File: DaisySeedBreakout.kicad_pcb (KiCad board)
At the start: 4 copper layers, 47.9 x 53.6 mm, 93 parts, among them J1 Conn_01x03, J10 Conn_01x03, J11 Conn_01x02, J12 Conn_01x02, J13 Conn_01x02, J14 Conn_01x03, J15 Conn_01x03, J16 Conn_01x02, J17 Conn_01x02, J2 Conn_01x02, J3 Conn_01x03, J4 5027740891, J5 Conn_02x08, J6 Pins_02x10_P2.54mm_TH, J7 Conn_01x10, J9 Conn_01x02, U1 H11L1M, U10 TPD2EUSB30ADRTR, U2 MAX4466EXK_T, U7 TLV9062IDR

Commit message: periodic update
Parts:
- removed C16: 10U, Capacitor_SMD:C_0805_2012Metric
- removed J7: Conn_01x10, Connector_PinHeader_2.54mm:PinHeader_1x10_P2.54mm_Vertical
- removed R29: 4.7k, Resistor_SMD:R_0402_1005Metric
- added J8: Conn_01x02, 1x2FemaleVertical:PinHeader_1x02_P2.54mm_VerticalFemale, F.Cu at (133.1, 60.3)
- C13, C7, D1, R21, R30, R54, R55: moved to B.Cu
- C15: value 10U -> 0.1uF; footprint Capacitor_SMD:C_0805_2012Metric -> Capacitor_SMD:C_0603_1608Metric
- C24, C70, C71, R66, R8, U3: moved to F.Cu
- J1, J10, J14, J3: footprint Ultralibrarian:PinHeader_1x03_P2.54mm_Vertical_Female -> HeadersWithSolderHoles:PinHeader_1x03_P2.54mm_Vertical_Female_WithSolderHoles
- J11, J12, J13, J17, J2: footprint 1x2FemaleVertical:PinHeader_1x02_P2.54mm_VerticalFemale -> HeadersWithSolderHoles:PinHeader_1x02_P2.54mm_VerticalFemale_WithSolderHoles
- J15: footprint Ultralibrarian:PinHeader_1x03_P2.54mm_Vertical_Female -> Connector_PinHeader_2.54mm:PinHeader_1x03_P2.54mm_Vertical
- J5: footprint Connector_PinHeader_2.54mm:PinHeader_2x08_P2.54mm_Vertical -> HeadersWithSolderHoles:PinHeader_2x08_P2.54mm_Vertical_Female
- J6: value Pins_02x10_P2.54mm_TH -> Conn_01x02; footprint Connector_PinHeader_2.54mm:PinHeader_2x10_P2.54mm_Vertical -> 1x2FemaleVertical:PinHeader_1x02_P2.54mm_VerticalFemale
- J9: value Conn_01x02 -> Pins_02x10_P2.54mm_TH; footprint 1x2FemaleVertical:PinHeader_1x02_P2.54mm_VerticalFemale -> HeadersWithSolderHoles:PinHeader_3x10_P2.54mm_Vertical
- moved J16 68.3 mm to (186.1, 88.3)
- moved C10 56.6 mm to (191.8, 97.0), turned to -90 degrees
- moved C6 45.7 mm to (112.4, 100.5)
- moved R11 41.6 mm to (102.7, 88.9)
- moved J12 41.4 mm to (130.6, 45.7), turned to 0 degrees
- moved J13 41.4 mm to (133.1, 45.7), turned to 0 degrees
- moved J5 38.5 mm to (157.5, 36.2)
- moved R52 35.7 mm to (116.6, 103.4)
- moved R53 35.7 mm to (116.3, 101.6)
- moved R6 34.9 mm to (108.4, 89.2)
- moved C15 32.4 mm to (143.3, 39.6), turned to -90 degrees
- moved J11 30.9 mm to (130.6, 73.2), turned to 0 degrees
- moved J1 29.2 mm to (137.2, 86.9)
- moved J2 28.9 mm to (133.1, 73.2), turned to 0 degrees
- moved J9 28.7 mm to (157.5, 56.5), turned to 0 degrees
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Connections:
- net /Audio In Sum/AUDIO_IN_L_CONN renamed /Audio In/AUDIO_IN_L_CONN
- net /Audio In Sum/AUDIO_IN_L_SUMMED renamed /Audio In/AUDIO_IN_L_SUMMED
- net /Audio In Sum/AUDIO_IN_R_CONN renamed /Audio In/AUDIO_IN_R_CONN
- net /Audio In Sum/AUDIO_IN_R_SUMMED renamed /Audio In/AUDIO_IN_R_SUMMED
- net Net-(C27-Pad2) renamed /Condensor Microphone/AUDIO_OUT
- A1 pad 39: unconnected-(A1-VIN-Pad39) -> Net-(A1-VIN)
- C15 pad 1: /Audio In Sum/AUDIO_IN_L_LOCAL -> Net-(A1-VIN)
- C15 pad 2: Net-(U7A-IN+) -> GND
- J15 pad 2: /USB_p -> /USB_n
- J15 pad 3: /USB_n -> /USB_p
- J6 pad 2: /AI_9 -> Net-(A1-VIN)
- J9 pad 1: /Audio In Sum/AUDIO_IN_R_LOCAL -> GND
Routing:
- net +3.3V: track 195.5 -> 6.27 mm, vias 7 -> 0
- net +3.3VA: track 101.7 -> 20.6 mm, vias 11 -> 2
- net /DIO6: track 49.9 -> 0.00 mm
- net /DIO7: track 45.8 -> 0.00 mm
- net /AI_0: track 43.4 -> 0.00 mm, vias 1 -> 0
- net /AI_2: track 42.5 -> 0.00 mm, vias 1 -> 0
- net GND: track 80.5 -> 38.7 mm, vias 44 -> 24
- net /AI_1: track 40.4 -> 0.00 mm, vias 1 -> 0
- net /AI_3: track 38.2 -> 0.00 mm, vias 1 -> 0
- net /AI_7: track 37.1 -> 0.00 mm, vias 1 -> 0
- net /AI_5: track 36.6 -> 0.00 mm, vias 1 -> 0
- net /AI_8: track 34.6 -> 0.00 mm, vias 1 -> 0
- net /AI_4: track 34.3 -> 0.00 mm, vias 1 -> 0
- net /AI_6: track 33.6 -> 0.00 mm, vias 1 -> 0
- net /DIO2: track 33.1 -> 0.54 mm
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- added copper zone on In1.Cu, net +3.3VA
- added copper zone on F.Cu, net GND
- removed copper zone on F.Cu, net +3.3V
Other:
- board size 47.9 x 53.6 mm -> 45.6 x 59.3 mm
- board text added: "AI0"
- board text added: "AI1"
- board text added: "AI2"
- board text added: "AI3"
- board text added: "AI4"
- board text added: "AI5"
- board text added: "AI6"
- board text added: "AI7"
- board text added: "AI8"
- board text added: "AI9"
- board text added: "AO0"
- board text added: "AO1"
- board text added: "D0/SCL/RX"
- board text added: "D1/SDA/TX"
- board text added: "D2/SPI_CS"
- board text added: "D3/SPI_CLK"
- board text added: "D4/SPI_POCI"
- board text added: "D5/SPI_PICO"
- board text added: "D6"
- board text added: "D7"
- board text added: "GND,VIN"
- board text added: "IN L"
- board text added: "IN R"
- board text added: "MIDI In"
- board text added: "MIDI Out"
- board text added: "Mic"
- board text added: "Mic Enable"
- board text added: "OUT L"
- board text added: "OUT R"
- board text added: "USB/TXRX"
- board text removed: "0 1 2 3 4 5 6 7 8 9 A B C D E F"
- board text removed: "7 6 5 4 3 2 1 0"
- board text removed: "9 8 7 6 5 4 3 2 1 0"
- board text removed: "Analog O"
- board text removed: "GND AI 3.3VA"
- board text removed: "GND AO 3.3V"
- board text removed: "GND AudI"
- board text removed: "GND AudIAux"
- board text removed: "GND AudO"
- board text removed: "GND, 3.3VD"
- board text removed: "L R"
- board text removed: "MIDI IN"
- board text removed: "MIDI OUT"
- board text removed: "Microphone"
- board text removed: "R"
- board text removed: "USB Host"

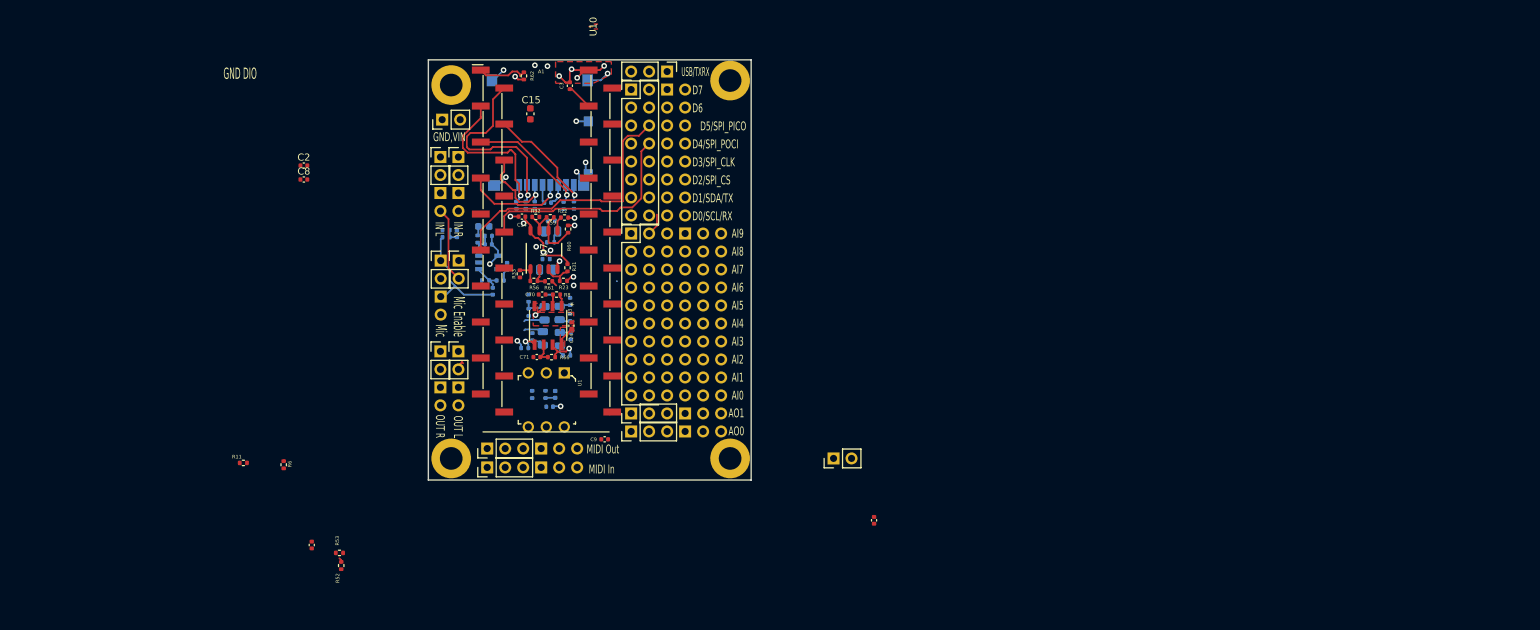
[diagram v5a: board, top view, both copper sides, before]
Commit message: added dedicated SPI, UART, I2C connectors
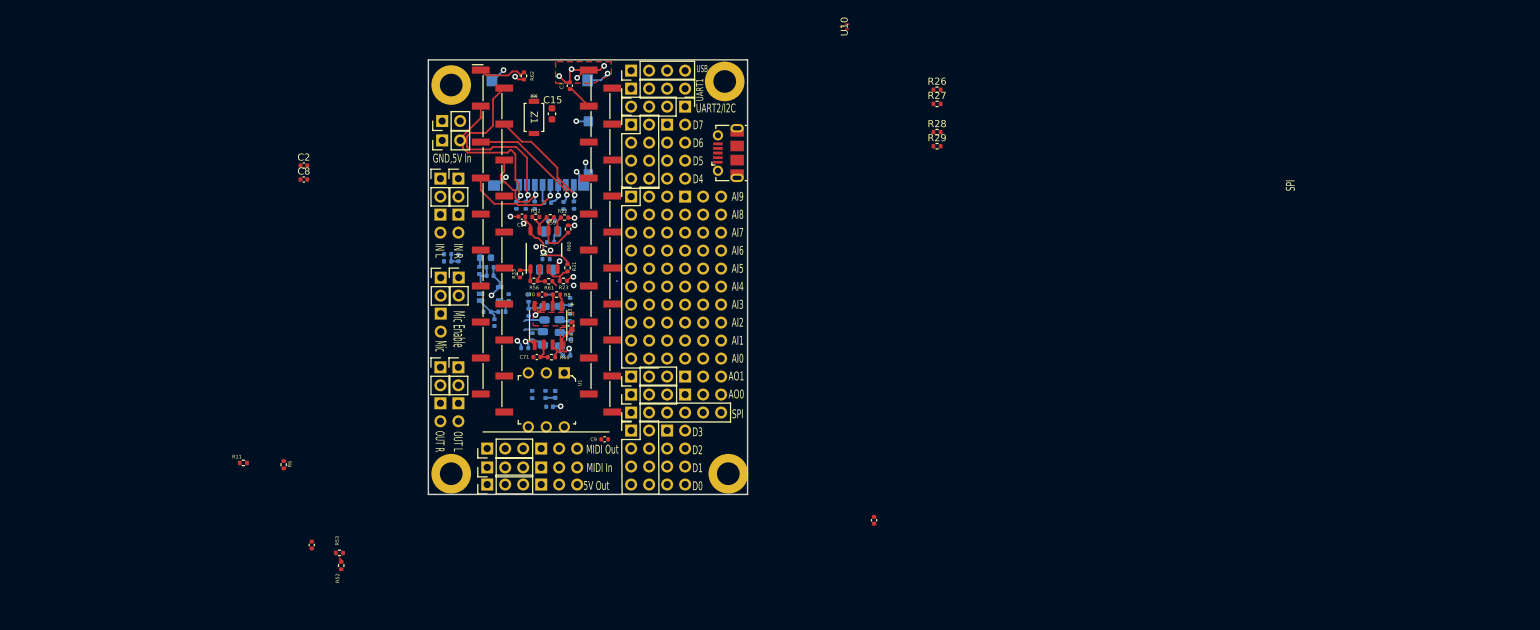
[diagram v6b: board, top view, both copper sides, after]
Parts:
- added J18: Conn_02x04, HeadersWithSolderHoles:PinHeader_2x04_P2.54mm_Vertical_Female, F.Cu at (157.5, 41.1)
- added J19: Conn_01x06, Ultralibrarian:PinHeader_1x06_P2.54mm_Vertical_Female, F.Cu at (157.5, 81.8)
- added J20: Conn_01x04, FemaleHeaders:PinHeader_1x04_P2.54mm_Vertical_Female, F.Cu at (157.5, 36.1)
- added J21: Conn_02x04, HeadersWithSolderHoles:PinHeader_2x04_P2.54mm_Vertical_Female, F.Cu at (157.5, 84.3)
- added J22: Conn_01x02, 1x2FemaleVertical:PinHeader_1x02_P2.54mm_VerticalFemale, F.Cu at (130.8, 43.4)
- added J7: Conn_01x04, FemaleHeaders:PinHeader_1x04_P2.54mm_Vertical_Female, F.Cu at (165.1, 38.6)
- added R26: DNP, Resistor_SMD:R_0402_1005Metric, F.Cu at (200.7, 36.2)
- added R27: DNP, Resistor_SMD:R_0402_1005Metric, F.Cu at (200.7, 38.2)
- added R28: DNP, Resistor_SMD:R_0402_1005Metric, F.Cu at (200.7, 42.2)
- added R29: DNP, Resistor_SMD:R_0402_1005Metric, F.Cu at (200.7, 44.2)
- added Z1: RSX501LAM20TR, 5ADiode:DIO_RB050LAM_ROM, F.Cu at (143.8, 40.1)
- J15: value Conn_01x03 -> USB_B_Micro; footprint Connector_PinHeader_2.54mm:PinHeader_1x03_P2.54mm_Vertical -> Connector_USB:USB_Micro-B_Molex-105017-0001
- J16: value Conn_01x02 -> Conn_01x03; footprint 1x2FemaleVertical:PinHeader_1x02_P2.54mm_VerticalFemale -> HeadersWithSolderHoles:PinHeader_1x03_P2.54mm_Vertical_Female_WithSolderHoles
- J5: value Conn_02x08 -> Conn_01x04; footprint HeadersWithSolderHoles:PinHeader_2x08_P2.54mm_Vertical_Female -> FemaleHeaders:PinHeader_1x04_P2.54mm_Vertical_Female
- moved J16 49.0 mm to (137.2, 91.9)
- moved U10 35.5 mm to (187.6, 27.3)
- moved J15 14.4 mm to (171.2, 45.2), turned to 90 degrees
- moved J14 5.21 mm to (157.5, 76.7)
- moved J9 5.21 mm to (157.5, 51.3)
- moved J10 5.21 mm to (157.5, 79.2)
- moved C28 4.43 mm to (136.9, 59.9)
- moved C23 4.43 mm to (140.2, 65.6)
- moved C27 4.43 mm to (137.6, 62.5)
- moved R17 4.43 mm to (137.6, 61.3)
- moved R20 4.43 mm to (136.0, 61.7)
- moved U2 4.43 mm to (137.6, 65.0)
- moved R16 4.43 mm to (137.2, 67.6)
- moved R15 4.43 mm to (139.2, 67.6)
- moved C26 4.43 mm to (138.2, 69.1)
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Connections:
- A1 pad 10: /DIO4 -> /DIO2_POCI
- A1 pad 11: /DIO5 -> /DIO3_PICO
- A1 pad 12: /DIO0 -> /DIO4_SCL_RX
- A1 pad 13: /DIO1 -> /DIO5_SDA_TX
- A1 pad 8: /DIO2 -> /DIO0_CS
- A1 pad 9: /DIO3 -> /DIO1_SCK
- J15 pad 1: GND -> unconnected-(J15-VBUS-Pad1)
- J15 pad 2: /USB_n -> unconnected-(J15-D--Pad2)
- J15 pad 3: /USB_p -> unconnected-(J15-D+-Pad3)
- J16 pad 1: GND -> +5V
- J16 pad 2: +3.3V -> +5V
- J5 pad 1: GND -> unconnected-(J5-Pin_1-Pad1)
- J5 pad 2: /DIO7 -> GND
- J5 pad 3: GND -> /USB_n
- J5 pad 4: /DIO6 -> /USB_p
- J6 pad 2: Net-(A1-VIN) -> Net-(J22-Pin_2)
- R11 pad 2: /DIO0 -> /DIO4_SCL_RX
- R6 pad 2: /DIO1 -> /DIO5_SDA_TX
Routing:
- net /DIO5: track 37.8 -> 0.00 mm
- net /DIO4: track 31.1 -> 0.00 mm
- net Net-(J17-Pin_1): track 16.3 -> 0.00 mm
- net /Audio In/AUDIO_IN_L_CONN: track 10.6 -> 0.00 mm
- net +3.3VA: track 20.6 -> 17.5 mm
- net GND: track 38.7 -> 38.2 mm, vias 24 -> 22
- net /DIO2: track 0.54 -> 0.00 mm
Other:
- board size 45.6 x 59.3 mm -> 45.1 x 61.3 mm
- board text added: "5V Out"
- board text added: "D0"
- board text added: "D1"
- board text added: "D2"
- board text added: "D3"
- board text added: "D4"
- board text added: "D5"
- board text added: "GND,5V In"
- board text added: "SPI"
- board text added: "UART1"
- board text added: "UART2/I2C"
- board text added: "USB"
- board text removed: "D0/SCL/RX"
- board text removed: "D1/SDA/TX"
- board text removed: "D2/SPI_CS"
- board text removed: "D3/SPI_CLK"
- board text removed: "D4/SPI_POCI"
- board text removed: "D5/SPI_PICO"
- board text removed: "GND DIO"
- board text removed: "GND,VIN"
- board text removed: "USB/TXRX"

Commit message: Layout routed, no DRC yet
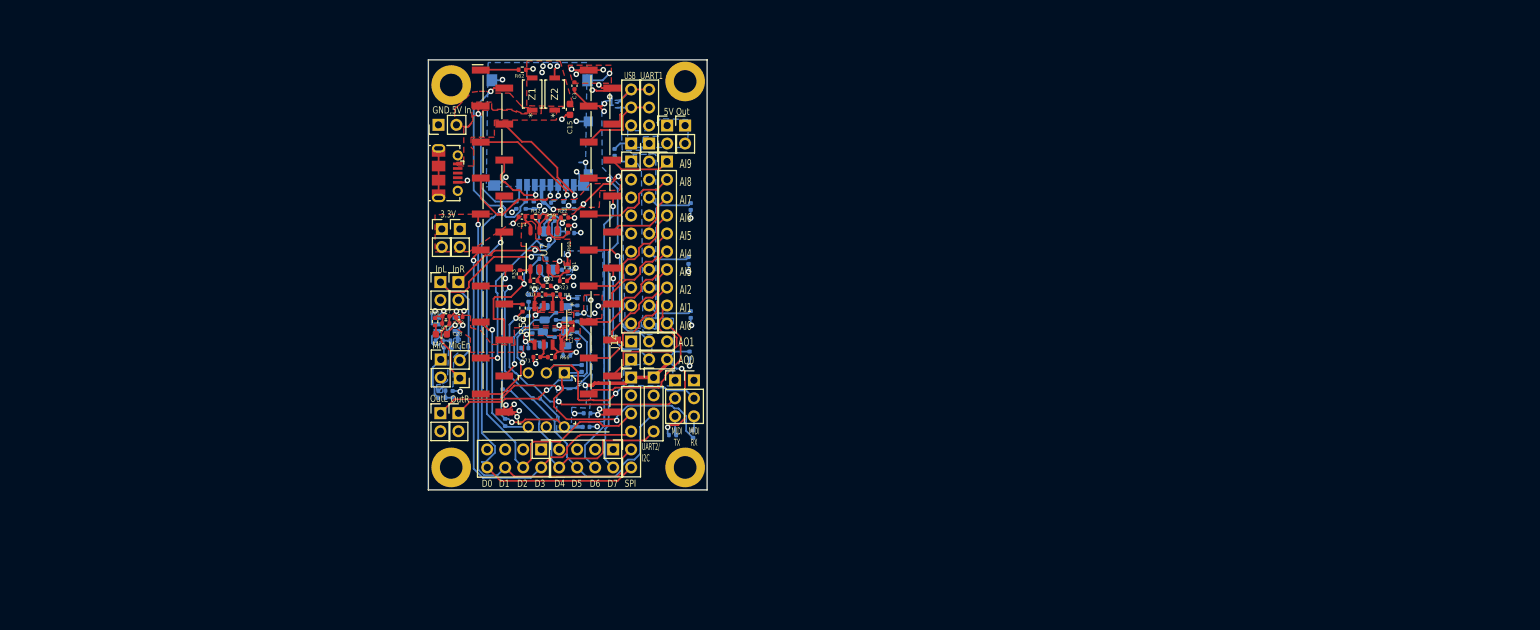
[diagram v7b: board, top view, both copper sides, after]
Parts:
- removed J22: Conn_01x02, 1x2FemaleVertical:PinHeader_1x02_P2.54mm_VerticalFemale
- added C16: 0.1uF, Capacitor_SMD:C_0402_1005Metric, B.Cu at (155.1, 45.1)
- added J23: Pins_02x10_P2.54mm_TH, 2x10FemaleHeader:PinHeader_2x10_P2.54mm_Vertical, F.Cu at (157.5, 46.4)
- added J24: Conn_01x10, Connector_PinHeader_2.54mm:PinHeader_1x10_P2.54mm_Vertical, F.Cu at (162.5, 46.4)
- added J25: Conn_01x02, 1x2FemaleVertical:PinHeader_1x02_P2.54mm_VerticalFemale, F.Cu at (130.8, 55.9)
- added J26: Conn_01x02, 1x2FemaleVertical:PinHeader_1x02_P2.54mm_VerticalFemale, F.Cu at (133.3, 55.9)
- added Z2: RSX501LAM20TR, 5ADiode:DIO_RB050LAM_ROM, F.Cu at (146.7, 36.8)
- C10, C2, C6, C8, C9, R11, R26, R27, R28, R29, R53, R6, U10: moved to B.Cu
- C23, C27, C28, R17, R20: moved to F.Cu
- J1, J10, J14, J3: footprint HeadersWithSolderHoles:PinHeader_1x03_P2.54mm_Vertical_Female_WithSolderHoles -> FemaleHeaders:PinHeader_1x03_P2.54mm_Vertical_Female
- J11, J12, J13, J17, J2: footprint HeadersWithSolderHoles:PinHeader_1x02_P2.54mm_VerticalFemale_WithSolderHoles -> 1x2FemaleVertical:PinHeader_1x02_P2.54mm_VerticalFemale
- J16: value Conn_01x03 -> Conn_01x02; footprint HeadersWithSolderHoles:PinHeader_1x03_P2.54mm_Vertical_Female_WithSolderHoles -> 1x2FemaleVertical:PinHeader_1x02_P2.54mm_VerticalFemale
- J18, J21: footprint HeadersWithSolderHoles:PinHeader_2x04_P2.54mm_Vertical_Female -> FemaleHeaders:PinHeader_2x04_P2.54mm_Vertical_Female
- J9: value Pins_02x10_P2.54mm_TH -> Conn_01x02; footprint HeadersWithSolderHoles:PinHeader_3x10_P2.54mm_Vertical -> 1x2FemaleVertical:PinHeader_1x02_P2.54mm_VerticalFemale
- moved C6 66.6 mm to (165.6, 60.3)
- moved R28 61.0 mm to (146.7, 70.6), turned to -90 degrees
- moved R26 60.5 mm to (145.0, 60.1)
- moved R29 58.9 mm to (146.9, 68.2), turned to 90 degrees
- moved R27 58.8 mm to (145.3, 58.2)
- moved J16 57.9 mm to (165.1, 41.3), turned to 0 degrees
- moved C8 57.8 mm to (165.9, 67.9), turned to -90 degrees
- moved C2 54.9 mm to (165.9, 52.7), turned to -90 degrees
- moved R53 49.9 mm to (163.3, 85.0), turned to 0 degrees
- moved J18 45.9 mm to (154.9, 87.0), turned to -90 degrees
- moved R52 44.5 mm to (142.2, 67.0), turned to -90 degrees
- moved J15 39.8 mm to (131.5, 48.0), turned to -90 degrees
- moved J7 38.5 mm to (160.7, 76.8), turned to 0 degrees
- moved R11 37.9 mm to (139.3, 79.0), turned to 90 degrees
- moved R6 36.9 mm to (144.1, 79.8), turned to 180 degrees
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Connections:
- A1 pad 39: Net-(A1-VIN) -> +5V
- C10 pad 1: +3.3VA -> +3.3V
- C15 pad 1: Net-(A1-VIN) -> +5V
- C2 pad 1: +3.3VA -> +3.3V
- C6 pad 1: +3.3VA -> +3.3V
- C8 pad 1: +3.3VA -> +3.3V
- J10 pad 3: +3.3VA -> +3.3V
- J14 pad 3: +3.3VA -> +3.3V
- J15 pad 1: unconnected-(J15-VBUS-Pad1) -> Net-(J15-VBUS)
- J5 pad 1: unconnected-(J5-Pin_1-Pad1) -> +5V
- J9 pad 1: GND -> +5V
- J9 pad 2: GND -> +5V
- U10 pad 1: /USB_n -> /USB_p
- U10 pad 2: /USB_p -> /USB_n
- Z1 pad 2: Net-(A1-VIN) -> +5V
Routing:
- net +3.3V: track 6.27 -> 99.8 mm, vias 0 -> 12
- net /DIO0_CS: track 0.00 -> 63.8 mm, vias 0 -> 1
- net /DIO1_SCK: track 0.00 -> 61.8 mm, vias 0 -> 1
- net /DIO3_PICO: track 0.00 -> 57.2 mm, vias 0 -> 1
- net /DIO2_POCI: track 0.00 -> 56.5 mm, vias 0 -> 1
- net /DIO5_SDA_TX: track 0.00 -> 51.5 mm, vias 0 -> 1
- net /DIO4_SCL_RX: track 0.00 -> 48.7 mm, vias 0 -> 1
- net /DIO7: track 0.00 -> 45.2 mm, vias 0 -> 1
- net GND: track 38.2 -> 82.0 mm, vias 22 -> 44
- net /DIO6: track 0.00 -> 40.6 mm, vias 0 -> 1
- net /Audio In/AUDIO_IN_L_CONN: track 0.00 -> 35.7 mm, vias 0 -> 1
- net Net-(J1-Pin_2): track 0.61 -> 34.5 mm, vias 0 -> 2
- net /Audio Out/AUDIO_OUT_L_EXT: track 2.08 -> 35.6 mm, vias 0 -> 1
- net Net-(D1-A): track 0.00 -> 33.0 mm, vias 0 -> 1
- net Net-(D1-K): track 1.39 -> 32.7 mm, vias 0 -> 1
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- added copper zone on B.Cu, net +3.3V
- added copper zone on F.Cu, net +3.3V
- added copper zone on B.Cu, net +3.3VA
- added copper zone on B.Cu, net +5V
- added copper zone on F.Cu, net +5V
- added copper zone on In2.Cu, net +5V
- added copper zone on B.Cu, net GND
- added copper zone on F.Cu, net Net-(J15-VBUS)
- added copper zone on F.Cu, net Net-(J6-Pin_2)
- removed copper zone on In1.Cu, net +3.3VA
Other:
- board size 45.1 x 61.3 mm -> 39.3 x 60.7 mm
- board text added: "3.3V"
- board text added: "InL"
- board text added: "InR"
- board text added: "MIDI RX"
- board text added: "MIDI TX"
- board text added: "MicEn"
- board text added: "OutL"
- board text added: "OutR"
- board text added: "UART2/ I2C"
- board text removed: "IN L"
- board text removed: "IN R"
- board text removed: "MIDI In"
- board text removed: "MIDI Out"
- board text removed: "Mic Enable"
- board text removed: "OUT L"
- board text removed: "OUT R"
- board text removed: "UART2/I2C"
